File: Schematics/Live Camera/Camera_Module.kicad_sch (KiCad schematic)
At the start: 92 parts, among them J1 Stack Male Edge Connector, J2 SWD_01x04_Pin, J4 Screw_Terminal_01x02, J4 USB_C_Female_USB2_Small, J5 VTX_DAT, J6 CAM_PWR, J7 CAM_DAT, J8 VTX_PWR, Q3 AO3400A, Q3 AO3401A, Q4 AO3400A, Q5 AO3401A, SW1 SW_STM_RESET, SW2 SW_STM_BOOT_MODE, U1 CP2102N-Axx-xQFN28, U1 LM66100DCKR, U1 STM32F103CBT6, U12 AMS1117-3.3, U3 W25Q128JVS, U5 LM66100DCKR, U6 LM66100DCKR, U8 ISO1042BDWVR, Y1 X322516MMB4SI

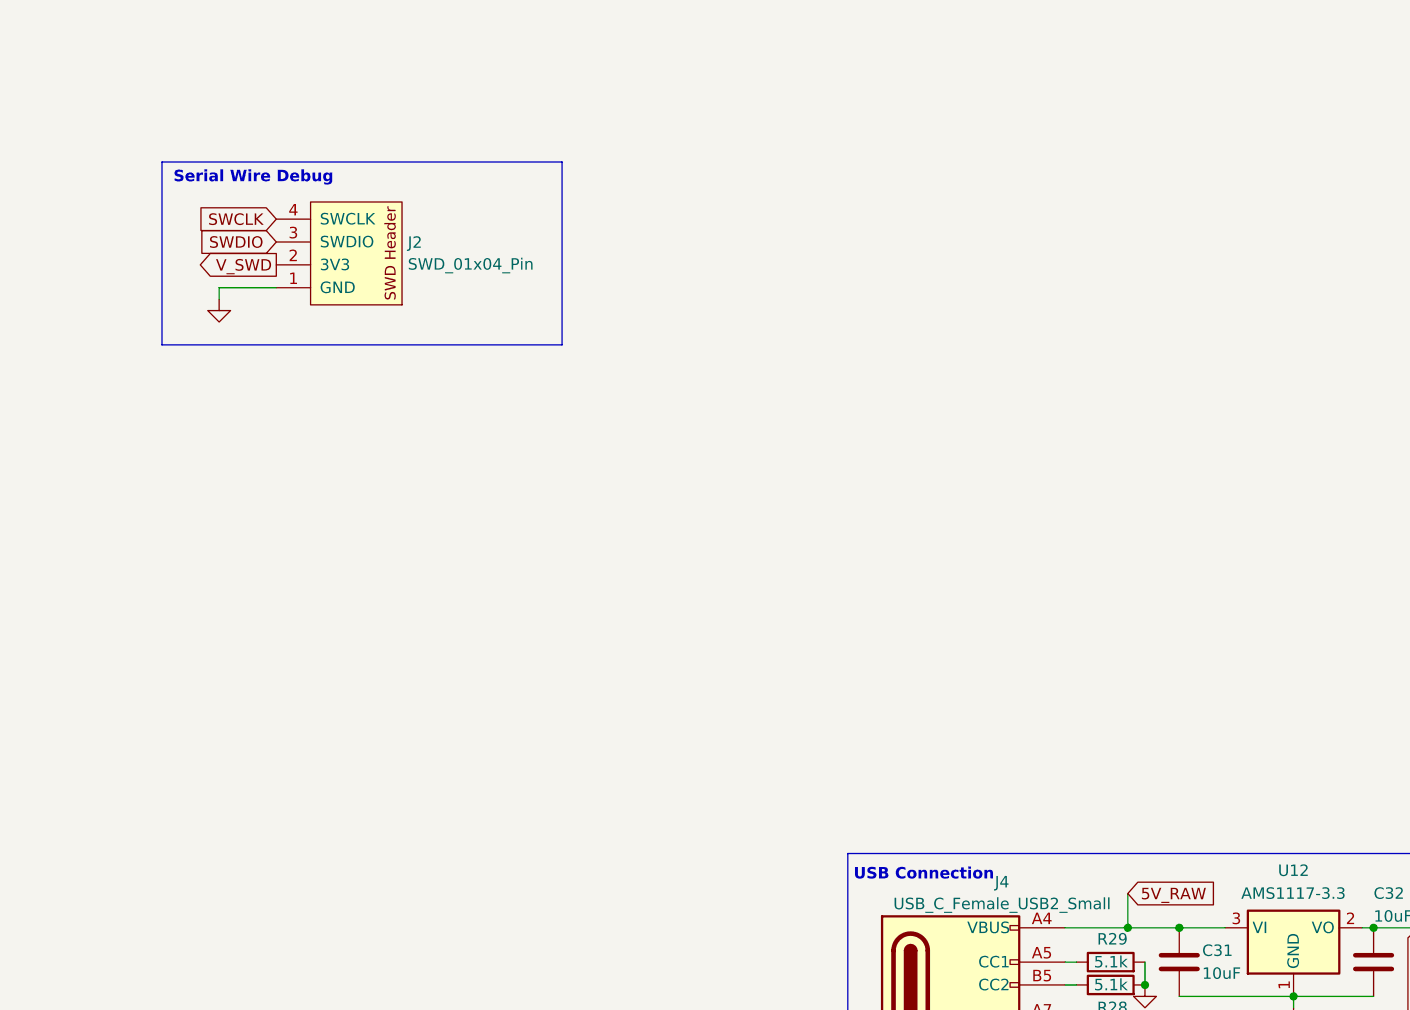
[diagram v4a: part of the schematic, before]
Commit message: Changed SWD header to SMD version
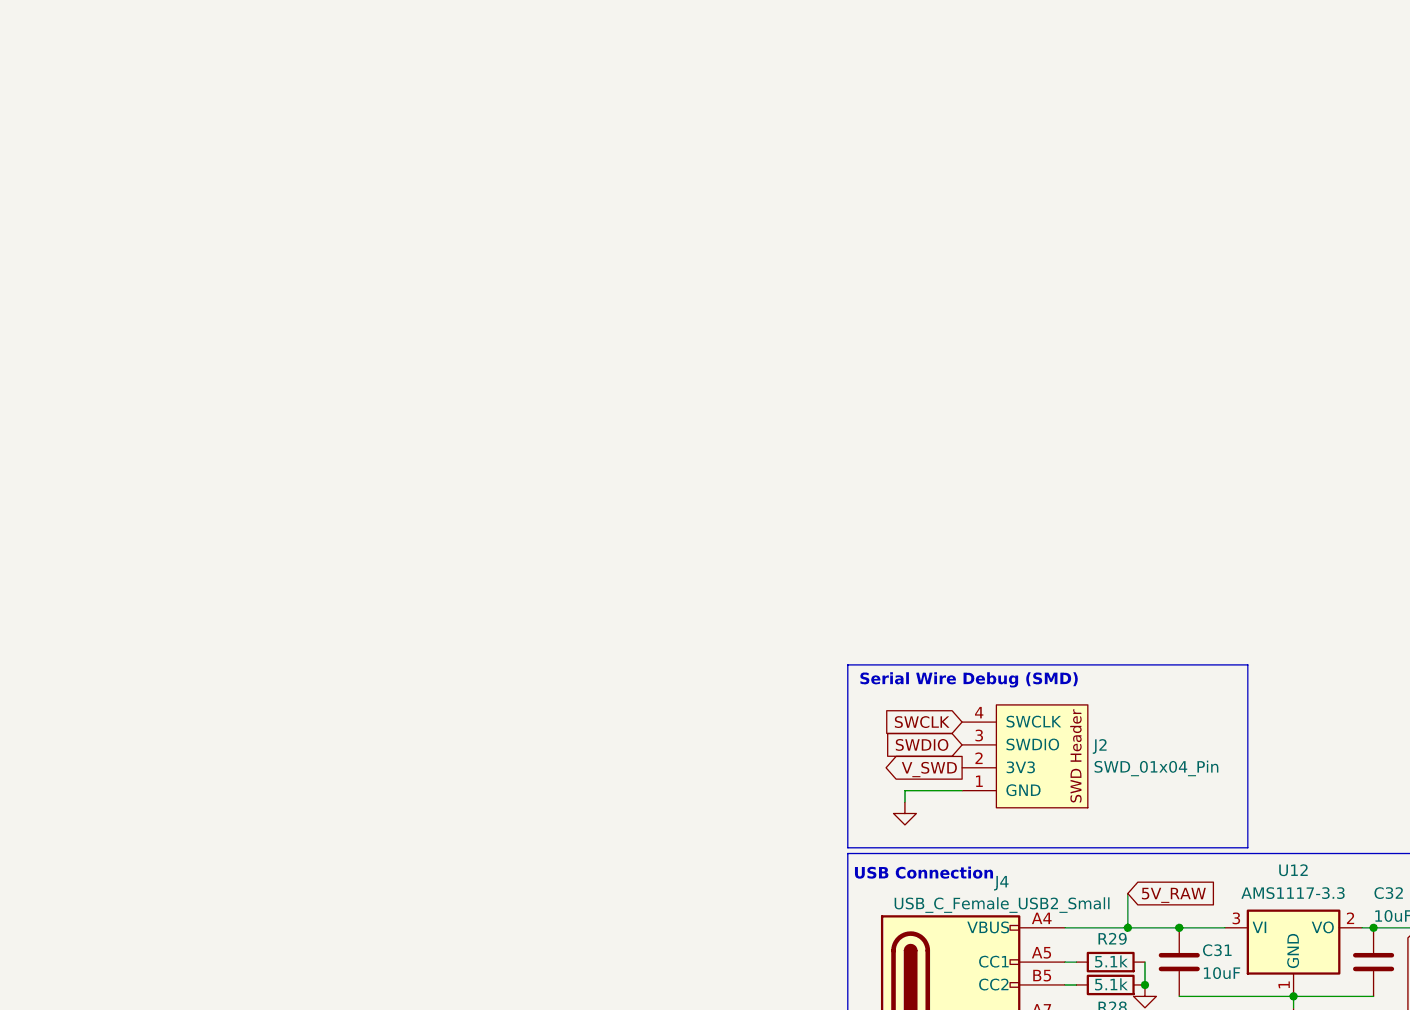
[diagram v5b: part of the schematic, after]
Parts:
- J2: footprint SWD_Header:SWD_PinHeader_1x04_P2.54mm_Horizontal -> SWD_Header:SWD_PinHeader_1x04_P2.54mm_Horizontal_SMD
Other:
- note added: "Serial Wire Debug (SMD)"
- note removed: "Serial Wire Debug"
- moved on the sheet: J2
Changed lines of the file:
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@@
 	(wire
 		(pts
-			(xy -57.15 160.655) (xy -57.15 161.925)
+			(xy 19.05 216.535) (xy 19.05 217.805)
 		)
 		(stroke
@@
 	(wire
 		(pts
-			(xy -57.15 160.655) (xy -50.8 160.655)
+			(xy 19.05 216.535) (xy 25.4 216.535)
 		)
 		(stroke
@@
 	(polyline
 		(pts
-			(xy -63.5 146.685) (xy -19.05 146.685)
+			(xy 12.7 202.565) (xy 57.15 202.565)
 		)
 		(stroke
@@
 	(polyline
 		(pts
-			(xy -63.5 167.005) (xy -63.5 146.685)
+			(xy 12.7 222.885) (xy 12.7 202.565)
 		)
 		(stroke
@@
 	(polyline
 		(pts
-			(xy -19.05 167.005) (xy -63.5 167.005)
+			(xy 57.15 222.885) (xy 12.7 222.885)
 		)
 		(stroke
@@
 	(polyline
 		(pts
-			(xy -19.05 146.685) (xy -19.05 167.005)
+			(xy 57.15 202.565) (xy 57.15 222.885)
 		)
 		(stroke
@@
 		)
 	)
-	(text "Serial Wire Debug"
+	(text "Serial Wire Debug (SMD)"
 		(exclude_from_sim no)
-		(at -62.23 149.225 0)
+		(at 13.97 205.105 0)
 		(effects
 			(font
@@
 	(global_label "SWDIO"
 		(shape input)
-		(at -50.8 155.575 180)
+		(at 25.4 211.455 180)
 		(fields_autoplaced yes)
 		(effects
@@
 		)
 		(property "Intersheetrefs" "${INTERSHEET_REFS}"
-			(at -59.6514 155.575 0)
+			(at 16.5486 211.455 0)
 			(effects
 				(font
@@
 	(global_label "V_SWD"
 		(shape output)
-		(at -50.8 158.115 180)
+		(at 25.4 213.995 180)
 		(fields_autoplaced yes)
 		(effects
@@
 		)
 		(property "Intersheetrefs" "${INTERSHEET_REFS}"
-			(at -59.7723 158.115 0)
+			(at 16.4277 213.995 0)
 			(effects
 				(font
@@
 	(global_label "SWCLK"
 		(shape input)
-		(at -50.8 153.035 180)
+		(at 25.4 208.915 180)
 		(fields_autoplaced yes)
 		(effects
@@
 		)
 		(property "Intersheetrefs" "${INTERSHEET_REFS}"
-			(at -60.0142 153.035 0)
+			(at 16.1858 208.915 0)
 			(effects
 				(font
@@
 	(symbol
 		(lib_id "EdgeConnector:SWD_01x04_Pin")
-		(at -45.72 158.115 180)
+		(at 30.48 213.995 180)
 		(unit 1)
 		(exclude_from_sim no)
@@
 		(fields_autoplaced yes)
 		(property "Reference" "J2"
-			(at -36.195 155.6329 0)
+			(at 40.005 211.5129 0)
 			(effects
 				(font
@@
 		)
 		(property "Value" "SWD_01x04_Pin"
-			(at -36.195 158.0571 0)
+			(at 40.005 213.9371 0)
 			(effects
 				(font
@@
 			)
 		)
-		(property "Footprint" "SWD_Header:SWD_PinHeader_1x04_P2.54mm_Horizontal"
-			(at -45.72 148.59 0)
+		(property "Footprint" "SWD_Header:SWD_PinHeader_1x04_P2.54mm_Horizontal_SMD"
+			(at 30.48 204.47 0)
 			(effects
 				(font
@@
 		)
 		(property "Datasheet" "~"
-			(at -36.83 149.86 0)
+			(at 39.37 205.74 0)
 			(effects
 				(font
@@
 		)
 		(property "Description" ""
-			(at -45.72 158.115 0)
+			(at 30.48 213.995 0)
 			(effects
 				(font
@@
 	(symbol
 		(lib_id "power:GND")
-		(at -57.15 161.925 0)
+		(at 19.05 217.805 0)
 		(unit 1)
 		(exclude_from_sim no)
@@
 		(fields_autoplaced yes)
 		(property "Reference" "#PWR048"
-			(at -57.15 168.275 0)
+			(at 19.05 224.155 0)
 			(effects
 				(font
@@
 		)
 		(property "Value" "GND"
-			(at -57.15 167.005 0)
+			(at 19.05 222.885 0)
 			(effects
 				(font
@@
 		)
 		(property "Footprint" ""
-			(at -57.15 161.925 0)
+			(at 19.05 217.805 0)
 			(effects
 				(font
@@
 		)
 		(property "Datasheet" ""
-			(at -57.15 161.925 0)
+			(at 19.05 217.805 0)
 			(effects
 				(font
@@
 		)
 		(property "Description" ""
-			(at -57.15 161.925 0)
+			(at 19.05 217.805 0)
 			(effects
 				(font

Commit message: Removed legacy RunCam6 PWM output
Also combined all RunCam6 interface pins to a single terminal block
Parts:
- removed J6: CAM_PWR, TerminalBlock_TE-Connectivity:TerminalBlock_TE_282834-2_1x02_P2.54mm_Horizontal, symbol Connector:Screw_Terminal_01x02
- removed J7: CAM_DAT, TerminalBlock_TE-Connectivity:TerminalBlock_TE_282834-3_1x03_P2.54mm_Horizontal, symbol Connector:Screw_Terminal_01x03
- added J6: RunCam6, TerminalBlock_TE-Connectivity:TerminalBlock_TE_282834-4_1x04_P2.54mm_Horizontal, symbol Connector:Screw_Terminal_01x04
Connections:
- net CAM_5V: now also J6.2 (Pin_2)
- net CAM_RX: now also J6.4 (Pin_4)
- net CAM_TX: now also J6.3 (Pin_3)
- net GND: now also J6.1 (Pin_1)
- net CAM_PWM: no longer names the net of U1.32 (PA11)
- no-connect marks 30 -> 31
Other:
- note added: "RunCam6 Control (Local Camera)"
- note added: "Runcam 6 draws ~450mA at worst w/ onboard battery full, assuming 1A when batt empty AO3401A: ~0.1R RDS(on), 4A max, suitable for ~1A no problem"
- note removed: "RunCam Control"
- moved on the sheet: C3, Q3, Q4, R10, R38, R39

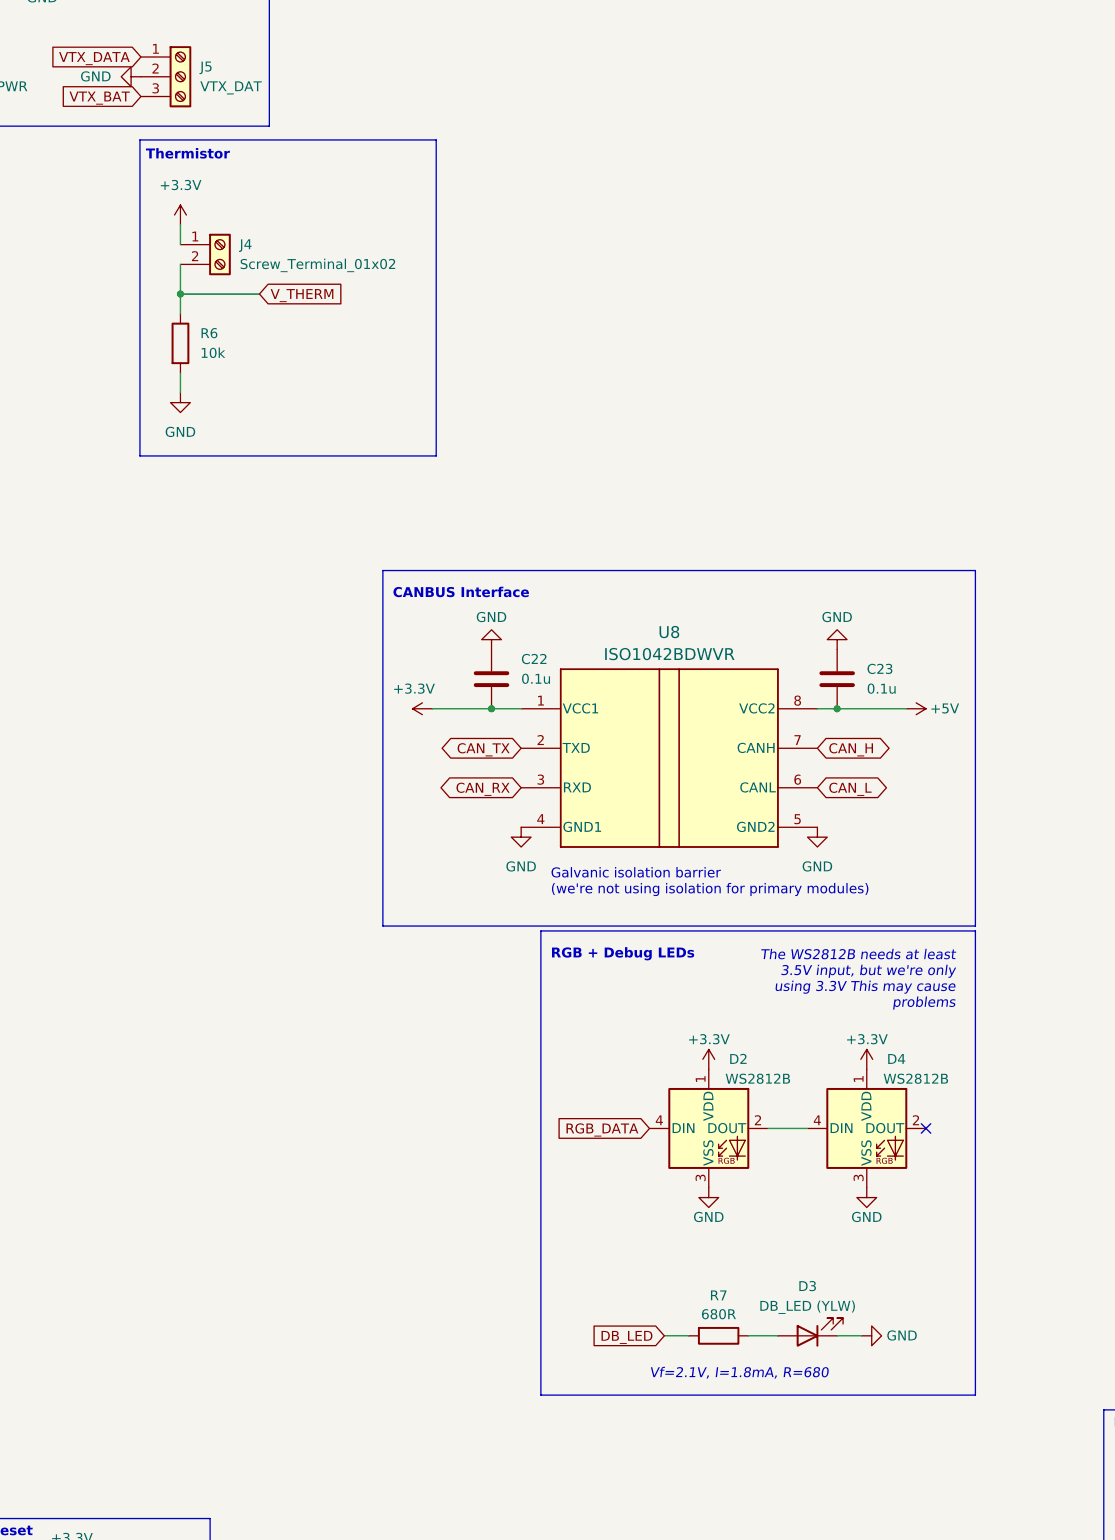
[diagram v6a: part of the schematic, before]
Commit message: Tweaked VTX thermistor circuit
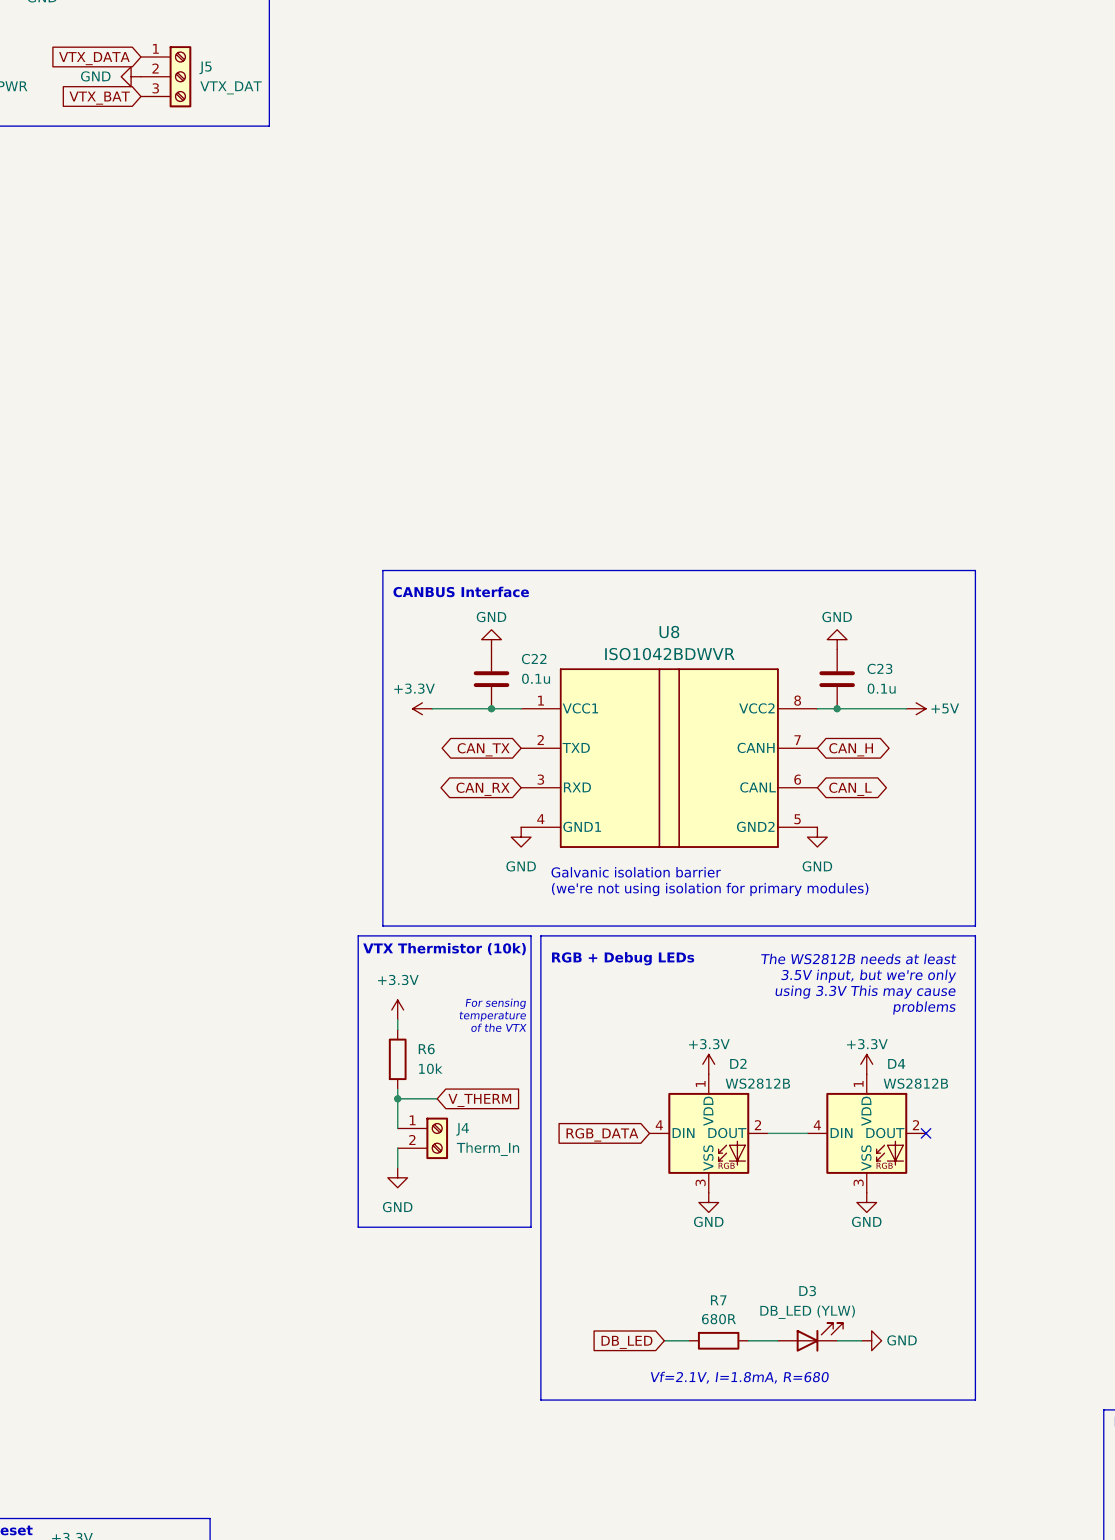
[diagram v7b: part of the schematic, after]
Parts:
- J4: value Screw_Terminal_01x02 -> Therm_In
- R6: footprint Resistor_SMD:R_0603_1608Metric -> Resistor_SMD:R_0603_1608Metric_Pad0.98x0.95mm_HandSolder
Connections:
- net +3.3V: now also R6.1; no longer J4.1 (Pin_1)
- net GND: now also J4.2 (Pin_2); no longer R6.2
- net V_THERM: now also J4.1 (Pin_1), R6.2; no longer J4.2 (Pin_2), R6.1
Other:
- note added: "For sensing temperature of the VTX"
- note added: "VTX Thermistor (10k)"
- note removed: "Thermistor"
- moved on the sheet: D2, D3, D4, J4, R6, R7
